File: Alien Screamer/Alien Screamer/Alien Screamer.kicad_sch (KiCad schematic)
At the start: 61 parts, among them J1 AudioJack2, Q1 2N3904, Q2 2N3904, Q3 Q_NJFET_DSG, SW1 PWR, SW2 LFO_Shaping, SW3 LFO_Shaping, SW4 SYNC, U1 LM324, U2 LM386

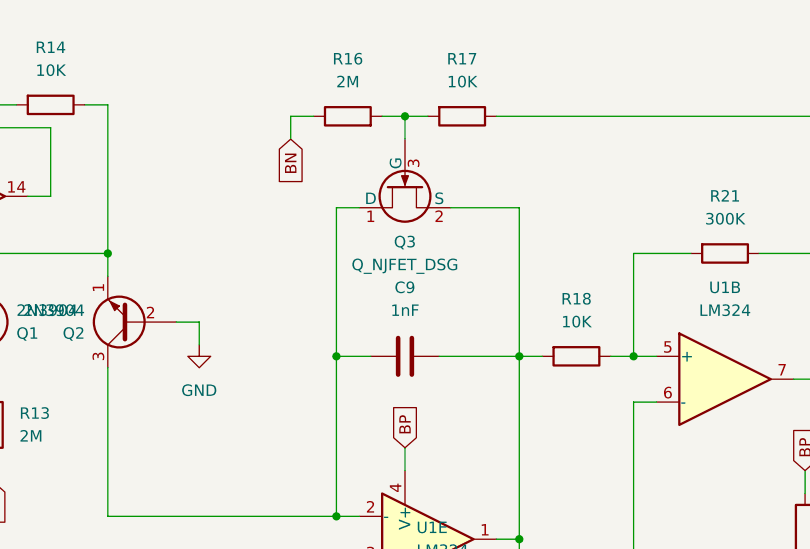
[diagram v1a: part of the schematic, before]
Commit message: Alien Screamer - changing resistor's sizes
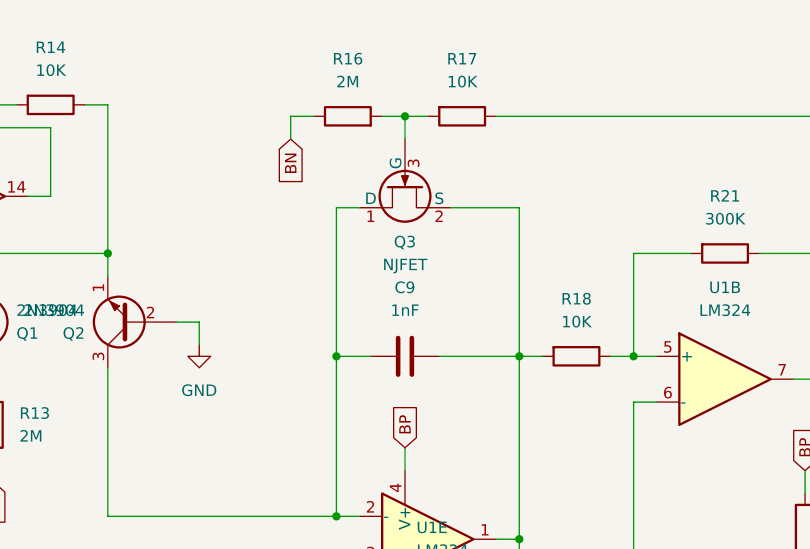
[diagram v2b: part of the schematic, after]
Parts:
- Q3: value Q_NJFET_DSG -> NJFET
- R1, R10, R11, R12, R13, R14, R15, R16, R17, R18, R19, R2, R20, R21, R22, R23, R24, R3, R4, R5, R6, R7, R8, R9: footprint Resistor_THT:R_Axial_DIN0204_L3.6mm_D1.6mm_P5.08mm_Horizontal -> Resistor_THT:R_Axial_DIN0207_L6.3mm_D2.5mm_P7.62mm_Horizontal
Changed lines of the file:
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@@
       (effects (font (size 1.27 1.27)) (justify left))
     )
-    (property "Footprint" "Resistor_THT:R_Axial_DIN0204_L3.6mm_D1.6mm_P5.08mm_Horizontal" (at 117.602 57.15 90)
+    (property "Footprint" "Resistor_THT:R_Axial_DIN0207_L6.3mm_D2.5mm_P7.62mm_Horizontal" (at 117.602 57.15 90)
       (effects (font (size 1.27 1.27)) hide)
     )
@@
       (effects (font (size 1.27 1.27)))
     )
-    (property "Footprint" "Resistor_THT:R_Axial_DIN0204_L3.6mm_D1.6mm_P5.08mm_Horizontal" (at 102.87 49.022 90)
+    (property "Footprint" "Resistor_THT:R_Axial_DIN0207_L6.3mm_D2.5mm_P7.62mm_Horizontal" (at 102.87 49.022 90)
       (effects (font (size 1.27 1.27)) hide)
     )
@@
       (effects (font (size 1.27 1.27)))
     )
-    (property "Footprint" "Resistor_THT:R_Axial_DIN0204_L3.6mm_D1.6mm_P5.08mm_Horizontal" (at 142.24 19.812 90)
+    (property "Footprint" "Resistor_THT:R_Axial_DIN0207_L6.3mm_D2.5mm_P7.62mm_Horizontal" (at 142.24 19.812 90)
       (effects (font (size 1.27 1.27)) hide)
     )
@@
       (effects (font (size 1.27 1.27)) (justify right))
     )
-    (property "Footprint" "Resistor_THT:R_Axial_DIN0204_L3.6mm_D1.6mm_P5.08mm_Horizontal" (at 18.288 63.5 90)
+    (property "Footprint" "Resistor_THT:R_Axial_DIN0207_L6.3mm_D2.5mm_P7.62mm_Horizontal" (at 18.288 63.5 90)
       (effects (font (size 1.27 1.27)) hide)
     )
@@
       (effects (font (size 1.27 1.27)) (justify right))
     )
-    (property "Footprint" "Resistor_THT:R_Axial_DIN0204_L3.6mm_D1.6mm_P5.08mm_Horizontal" (at 50.038 180.34 90)
+    (property "Footprint" "Resistor_THT:R_Axial_DIN0207_L6.3mm_D2.5mm_P7.62mm_Horizontal" (at 50.038 180.34 90)
       (effects (font (size 1.27 1.27)) hide)
     )
@@
       (effects (font (size 1.27 1.27)) (justify right))
     )
-    (property "Footprint" "Resistor_THT:R_Axial_DIN0204_L3.6mm_D1.6mm_P5.08mm_Horizontal" (at 227.838 78.74 90)
+    (property "Footprint" "Resistor_THT:R_Axial_DIN0207_L6.3mm_D2.5mm_P7.62mm_Horizontal" (at 227.838 78.74 90)
       (effects (font (size 1.27 1.27)) hide)
     )
@@
       (effects (font (size 1.27 1.27)))
     )
-    (property "Footprint" "Resistor_THT:R_Axial_DIN0204_L3.6mm_D1.6mm_P5.08mm_Horizontal" (at 200.66 47.752 90)
+    (property "Footprint" "Resistor_THT:R_Axial_DIN0207_L6.3mm_D2.5mm_P7.62mm_Horizontal" (at 200.66 47.752 90)
       (effects (font (size 1.27 1.27)) hide)
     )
@@
       (effects (font (size 1.27 1.27)))
     )
-    (property "Footprint" "Resistor_THT:R_Axial_DIN0204_L3.6mm_D1.6mm_P5.08mm_Horizontal" (at 175.26 24.638 90)
+    (property "Footprint" "Resistor_THT:R_Axial_DIN0207_L6.3mm_D2.5mm_P7.62mm_Horizontal" (at 175.26 24.638 90)
       (effects (font (size 1.27 1.27)) hide)
     )
@@
       (effects (font (size 1.27 1.27)) (justify left))
     )
-    (property "Footprint" "Resistor_THT:R_Axial_DIN0204_L3.6mm_D1.6mm_P5.08mm_Horizontal" (at 107.442 57.15 90)
+    (property "Footprint" "Resistor_THT:R_Axial_DIN0207_L6.3mm_D2.5mm_P7.62mm_Horizontal" (at 107.442 57.15 90)
       (effects (font (size 1.27 1.27)) hide)
     )
@@
       (effects (font (size 1.27 1.27)) (justify right))
     )
-    (property "Footprint" "Resistor_THT:R_Axial_DIN0204_L3.6mm_D1.6mm_P5.08mm_Horizontal" (at 251.968 151.13 90)
+    (property "Footprint" "Resistor_THT:R_Axial_DIN0207_L6.3mm_D2.5mm_P7.62mm_Horizontal" (at 251.968 151.13 90)
       (effects (font (size 1.27 1.27)) hide)
     )
@@
       (effects (font (size 1.27 1.27)) (justify right))
     )
-    (property "Footprint" "Resistor_THT:R_Axial_DIN0204_L3.6mm_D1.6mm_P5.08mm_Horizontal" (at 227.838 68.58 90)
+    (property "Footprint" "Resistor_THT:R_Axial_DIN0207_L6.3mm_D2.5mm_P7.62mm_Horizontal" (at 227.838 68.58 90)
       (effects (font (size 1.27 1.27)) hide)
     )
@@
       (effects (font (size 1.27 1.27)))
     )
-    (property "Footprint" "Resistor_THT:R_Axial_DIN0204_L3.6mm_D1.6mm_P5.08mm_Horizontal" (at 62.23 50.292 90)
+    (property "Footprint" "Resistor_THT:R_Axial_DIN0207_L6.3mm_D2.5mm_P7.62mm_Horizontal" (at 62.23 50.292 90)
       (effects (font (size 1.27 1.27)) hide)
     )
@@
       (effects (font (size 1.27 1.27)))
     )
-    (property "Footprint" "Resistor_THT:R_Axial_DIN0204_L3.6mm_D1.6mm_P5.08mm_Horizontal" (at 102.87 22.352 90)
+    (property "Footprint" "Resistor_THT:R_Axial_DIN0207_L6.3mm_D2.5mm_P7.62mm_Horizontal" (at 102.87 22.352 90)
       (effects (font (size 1.27 1.27)) hide)
     )
@@
       (effects (font (size 1.27 1.27)))
     )
-    (property "Footprint" "Resistor_THT:R_Axial_DIN0204_L3.6mm_D1.6mm_P5.08mm_Horizontal" (at 31.75 23.368 90)
+    (property "Footprint" "Resistor_THT:R_Axial_DIN0207_L6.3mm_D2.5mm_P7.62mm_Horizontal" (at 31.75 23.368 90)
       (effects (font (size 1.27 1.27)) hide)
     )
@@
       (effects (font (size 1.27 1.27)) (justify left))
     )
-    (property "Footprint" "Resistor_THT:R_Axial_DIN0204_L3.6mm_D1.6mm_P5.08mm_Horizontal" (at 134.112 57.15 90)
+    (property "Footprint" "Resistor_THT:R_Axial_DIN0207_L6.3mm_D2.5mm_P7.62mm_Horizontal" (at 134.112 57.15 90)
       (effects (font (size 1.27 1.27)) hide)
     )
@@
       (effects (font (size 1.27 1.27)) (justify right))
     )
-    (property "Footprint" "Resistor_THT:R_Axial_DIN0204_L3.6mm_D1.6mm_P5.08mm_Horizontal" (at 39.878 64.77 90)
+    (property "Footprint" "Resistor_THT:R_Axial_DIN0207_L6.3mm_D2.5mm_P7.62mm_Horizontal" (at 39.878 64.77 90)
       (effects (font (size 1.27 1.27)) hide)
     )
@@
       (effects (font (size 1.27 1.27)))
     )
-    (property "Footprint" "Resistor_THT:R_Axial_DIN0204_L3.6mm_D1.6mm_P5.08mm_Horizontal" (at 31.75 56.642 90)
+    (property "Footprint" "Resistor_THT:R_Axial_DIN0207_L6.3mm_D2.5mm_P7.62mm_Horizontal" (at 31.75 56.642 90)
       (effects (font (size 1.27 1.27)) hide)
     )
@@
       (effects (font (size 1.27 1.27)))
     )
-    (property "Footprint" "Resistor_THT:R_Axial_DIN0204_L3.6mm_D1.6mm_P5.08mm_Horizontal" (at 217.17 36.322 90)
+    (property "Footprint" "Resistor_THT:R_Axial_DIN0207_L6.3mm_D2.5mm_P7.62mm_Horizontal" (at 217.17 36.322 90)
       (effects (font (size 1.27 1.27)) hide)
     )
@@
       (effects (font (size 1.27 1.27)) (justify right))
     )
-    (property "Footprint" "Resistor_THT:R_Axial_DIN0204_L3.6mm_D1.6mm_P5.08mm_Horizontal" (at 213.868 138.43 90)
+    (property "Footprint" "Resistor_THT:R_Axial_DIN0207_L6.3mm_D2.5mm_P7.62mm_Horizontal" (at 213.868 138.43 90)
       (effects (font (size 1.27 1.27)) hide)
     )
@@
       (effects (font (size 1.27 1.27)) (justify right))
     )
-    (property "Footprint" "Resistor_THT:R_Axial_DIN0204_L3.6mm_D1.6mm_P5.08mm_Horizontal" (at 18.288 53.34 90)
+    (property "Footprint" "Resistor_THT:R_Axial_DIN0207_L6.3mm_D2.5mm_P7.62mm_Horizontal" (at 18.288 53.34 90)
       (effects (font (size 1.27 1.27)) hide)
     )
@@
       (effects (font (size 1.27 1.27)) (justify right))
     )
-    (property "Footprint" "Resistor_THT:R_Axial_DIN0204_L3.6mm_D1.6mm_P5.08mm_Horizontal" (at 144.018 96.52 90)
+    (property "Footprint" "Resistor_THT:R_Axial_DIN0207_L6.3mm_D2.5mm_P7.62mm_Horizontal" (at 144.018 96.52 90)
       (effects (font (size 1.27 1.27)) hide)
     )
@@
       (effects (font (size 1.27 1.27)))
     )
-    (property "Value" "Q_NJFET_DSG" (at 181.61 39.37 90)
+    (property "Value" "NJFET" (at 181.61 39.37 90)
       (effects (font (size 1.27 1.27)))
     )
@@
       (effects (font (size 1.27 1.27)) (justify right))
     )
-    (property "Footprint" "Resistor_THT:R_Axial_DIN0204_L3.6mm_D1.6mm_P5.08mm_Horizontal" (at 50.038 165.1 90)
+    (property "Footprint" "Resistor_THT:R_Axial_DIN0207_L6.3mm_D2.5mm_P7.62mm_Horizontal" (at 50.038 165.1 90)
       (effects (font (size 1.27 1.27)) hide)
     )
@@
       (effects (font (size 1.27 1.27)))
     )
-    (property "Footprint" "Resistor_THT:R_Axial_DIN0204_L3.6mm_D1.6mm_P5.08mm_Horizontal" (at 205.74 130.302 90)
+    (property "Footprint" "Resistor_THT:R_Axial_DIN0207_L6.3mm_D2.5mm_P7.62mm_Horizontal" (at 205.74 130.302 90)
       (effects (font (size 1.27 1.27)) hide)
     )
@@
       (effects (font (size 1.27 1.27)))
     )
-    (property "Footprint" "Resistor_THT:R_Axial_DIN0204_L3.6mm_D1.6mm_P5.08mm_Horizontal" (at 187.96 21.082 90)
-      (effects (font (size 1.27 1.27)) hide)
-    )
+    (property "Footprint" "Resistor_THT:R_Axial_DIN0207_L6.3mm_D2.5mm_P7.62mm_Horizontal" (at 187.96 21.082 90)
+      (effects (font (size 1.27 1.27)) hide)
+    )

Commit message: Alien Screamer - changed resistors sizes
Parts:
- R1, R10, R11, R12, R13, R14, R15, R16, R17, R18, R19, R2, R20, R21, R22, R23, R24, R3, R4, R5, R6, R7, R8, R9: footprint Resistor_THT:R_Axial_DIN0207_L6.3mm_D2.5mm_P7.62mm_Horizontal -> Library:R_Axial_DIN0207_L6.3mm_D2.5mm_P7.62mm_Horizontal
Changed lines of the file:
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@@
       (effects (font (size 1.27 1.27)) (justify left))
     )
-    (property "Footprint" "Resistor_THT:R_Axial_DIN0207_L6.3mm_D2.5mm_P7.62mm_Horizontal" (at 117.602 57.15 90)
+    (property "Footprint" "Library:R_Axial_DIN0207_L6.3mm_D2.5mm_P7.62mm_Horizontal" (at 117.602 57.15 90)
       (effects (font (size 1.27 1.27)) hide)
     )
@@
       (effects (font (size 1.27 1.27)))
     )
-    (property "Footprint" "Resistor_THT:R_Axial_DIN0207_L6.3mm_D2.5mm_P7.62mm_Horizontal" (at 102.87 49.022 90)
+    (property "Footprint" "Library:R_Axial_DIN0207_L6.3mm_D2.5mm_P7.62mm_Horizontal" (at 102.87 49.022 90)
       (effects (font (size 1.27 1.27)) hide)
     )
@@
       (effects (font (size 1.27 1.27)))
     )
-    (property "Footprint" "Resistor_THT:R_Axial_DIN0207_L6.3mm_D2.5mm_P7.62mm_Horizontal" (at 142.24 19.812 90)
+    (property "Footprint" "Library:R_Axial_DIN0207_L6.3mm_D2.5mm_P7.62mm_Horizontal" (at 142.24 19.812 90)
       (effects (font (size 1.27 1.27)) hide)
     )
@@
       (effects (font (size 1.27 1.27)) (justify right))
     )
-    (property "Footprint" "Resistor_THT:R_Axial_DIN0207_L6.3mm_D2.5mm_P7.62mm_Horizontal" (at 18.288 63.5 90)
+    (property "Footprint" "Library:R_Axial_DIN0207_L6.3mm_D2.5mm_P7.62mm_Horizontal" (at 18.288 63.5 90)
       (effects (font (size 1.27 1.27)) hide)
     )
@@
       (effects (font (size 1.27 1.27)) (justify right))
     )
-    (property "Footprint" "Resistor_THT:R_Axial_DIN0207_L6.3mm_D2.5mm_P7.62mm_Horizontal" (at 50.038 180.34 90)
+    (property "Footprint" "Library:R_Axial_DIN0207_L6.3mm_D2.5mm_P7.62mm_Horizontal" (at 50.038 180.34 90)
       (effects (font (size 1.27 1.27)) hide)
     )
@@
       (effects (font (size 1.27 1.27)) (justify right))
     )
-    (property "Footprint" "Resistor_THT:R_Axial_DIN0207_L6.3mm_D2.5mm_P7.62mm_Horizontal" (at 227.838 78.74 90)
+    (property "Footprint" "Library:R_Axial_DIN0207_L6.3mm_D2.5mm_P7.62mm_Horizontal" (at 227.838 78.74 90)
       (effects (font (size 1.27 1.27)) hide)
     )
@@
       (effects (font (size 1.27 1.27)))
     )
-    (property "Footprint" "Resistor_THT:R_Axial_DIN0207_L6.3mm_D2.5mm_P7.62mm_Horizontal" (at 200.66 47.752 90)
+    (property "Footprint" "Library:R_Axial_DIN0207_L6.3mm_D2.5mm_P7.62mm_Horizontal" (at 200.66 47.752 90)
       (effects (font (size 1.27 1.27)) hide)
     )
@@
       (effects (font (size 1.27 1.27)))
     )
-    (property "Footprint" "Resistor_THT:R_Axial_DIN0207_L6.3mm_D2.5mm_P7.62mm_Horizontal" (at 175.26 24.638 90)
+    (property "Footprint" "Library:R_Axial_DIN0207_L6.3mm_D2.5mm_P7.62mm_Horizontal" (at 175.26 24.638 90)
       (effects (font (size 1.27 1.27)) hide)
     )
@@
       (effects (font (size 1.27 1.27)) (justify left))
     )
-    (property "Footprint" "Resistor_THT:R_Axial_DIN0207_L6.3mm_D2.5mm_P7.62mm_Horizontal" (at 107.442 57.15 90)
+    (property "Footprint" "Library:R_Axial_DIN0207_L6.3mm_D2.5mm_P7.62mm_Horizontal" (at 107.442 57.15 90)
       (effects (font (size 1.27 1.27)) hide)
     )
@@
       (effects (font (size 1.27 1.27)) (justify right))
     )
-    (property "Footprint" "Resistor_THT:R_Axial_DIN0207_L6.3mm_D2.5mm_P7.62mm_Horizontal" (at 251.968 151.13 90)
+    (property "Footprint" "Library:R_Axial_DIN0207_L6.3mm_D2.5mm_P7.62mm_Horizontal" (at 251.968 151.13 90)
       (effects (font (size 1.27 1.27)) hide)
     )
@@
       (effects (font (size 1.27 1.27)) (justify right))
     )
-    (property "Footprint" "Resistor_THT:R_Axial_DIN0207_L6.3mm_D2.5mm_P7.62mm_Horizontal" (at 227.838 68.58 90)
+    (property "Footprint" "Library:R_Axial_DIN0207_L6.3mm_D2.5mm_P7.62mm_Horizontal" (at 227.838 68.58 90)
       (effects (font (size 1.27 1.27)) hide)
     )
@@
       (effects (font (size 1.27 1.27)))
     )
-    (property "Footprint" "Resistor_THT:R_Axial_DIN0207_L6.3mm_D2.5mm_P7.62mm_Horizontal" (at 62.23 50.292 90)
+    (property "Footprint" "Library:R_Axial_DIN0207_L6.3mm_D2.5mm_P7.62mm_Horizontal" (at 62.23 50.292 90)
       (effects (font (size 1.27 1.27)) hide)
     )
@@
       (effects (font (size 1.27 1.27)))
     )
-    (property "Footprint" "Resistor_THT:R_Axial_DIN0207_L6.3mm_D2.5mm_P7.62mm_Horizontal" (at 102.87 22.352 90)
+    (property "Footprint" "Library:R_Axial_DIN0207_L6.3mm_D2.5mm_P7.62mm_Horizontal" (at 102.87 22.352 90)
       (effects (font (size 1.27 1.27)) hide)
     )
@@
       (effects (font (size 1.27 1.27)))
     )
-    (property "Footprint" "Resistor_THT:R_Axial_DIN0207_L6.3mm_D2.5mm_P7.62mm_Horizontal" (at 31.75 23.368 90)
+    (property "Footprint" "Library:R_Axial_DIN0207_L6.3mm_D2.5mm_P7.62mm_Horizontal" (at 31.75 23.368 90)
       (effects (font (size 1.27 1.27)) hide)
     )
@@
       (effects (font (size 1.27 1.27)) (justify left))
     )
-    (property "Footprint" "Resistor_THT:R_Axial_DIN0207_L6.3mm_D2.5mm_P7.62mm_Horizontal" (at 134.112 57.15 90)
+    (property "Footprint" "Library:R_Axial_DIN0207_L6.3mm_D2.5mm_P7.62mm_Horizontal" (at 134.112 57.15 90)
       (effects (font (size 1.27 1.27)) hide)
     )
@@
       (effects (font (size 1.27 1.27)) (justify right))
     )
-    (property "Footprint" "Resistor_THT:R_Axial_DIN0207_L6.3mm_D2.5mm_P7.62mm_Horizontal" (at 39.878 64.77 90)
+    (property "Footprint" "Library:R_Axial_DIN0207_L6.3mm_D2.5mm_P7.62mm_Horizontal" (at 39.878 64.77 90)
       (effects (font (size 1.27 1.27)) hide)
     )
@@
       (effects (font (size 1.27 1.27)))
     )
-    (property "Footprint" "Resistor_THT:R_Axial_DIN0207_L6.3mm_D2.5mm_P7.62mm_Horizontal" (at 31.75 56.642 90)
+    (property "Footprint" "Library:R_Axial_DIN0207_L6.3mm_D2.5mm_P7.62mm_Horizontal" (at 31.75 56.642 90)
       (effects (font (size 1.27 1.27)) hide)
     )
@@
       (effects (font (size 1.27 1.27)))
     )
-    (property "Footprint" "Resistor_THT:R_Axial_DIN0207_L6.3mm_D2.5mm_P7.62mm_Horizontal" (at 217.17 36.322 90)
+    (property "Footprint" "Library:R_Axial_DIN0207_L6.3mm_D2.5mm_P7.62mm_Horizontal" (at 217.17 36.322 90)
       (effects (font (size 1.27 1.27)) hide)
     )
@@
       (effects (font (size 1.27 1.27)) (justify right))
     )
-    (property "Footprint" "Resistor_THT:R_Axial_DIN0207_L6.3mm_D2.5mm_P7.62mm_Horizontal" (at 213.868 138.43 90)
+    (property "Footprint" "Library:R_Axial_DIN0207_L6.3mm_D2.5mm_P7.62mm_Horizontal" (at 213.868 138.43 90)
       (effects (font (size 1.27 1.27)) hide)
     )
@@
       (effects (font (size 1.27 1.27)) (justify right))
     )
-    (property "Footprint" "Resistor_THT:R_Axial_DIN0207_L6.3mm_D2.5mm_P7.62mm_Horizontal" (at 18.288 53.34 90)
+    (property "Footprint" "Library:R_Axial_DIN0207_L6.3mm_D2.5mm_P7.62mm_Horizontal" (at 18.288 53.34 90)
       (effects (font (size 1.27 1.27)) hide)
     )
@@
       (effects (font (size 1.27 1.27)) (justify right))
     )
-    (property "Footprint" "Resistor_THT:R_Axial_DIN0207_L6.3mm_D2.5mm_P7.62mm_Horizontal" (at 144.018 96.52 90)
+    (property "Footprint" "Library:R_Axial_DIN0207_L6.3mm_D2.5mm_P7.62mm_Horizontal" (at 144.018 96.52 90)
       (effects (font (size 1.27 1.27)) hide)
     )
@@
       (effects (font (size 1.27 1.27)) (justify right))
     )
-    (property "Footprint" "Resistor_THT:R_Axial_DIN0207_L6.3mm_D2.5mm_P7.62mm_Horizontal" (at 50.038 165.1 90)
+    (property "Footprint" "Library:R_Axial_DIN0207_L6.3mm_D2.5mm_P7.62mm_Horizontal" (at 50.038 165.1 90)
       (effects (font (size 1.27 1.27)) hide)
     )
@@
       (effects (font (size 1.27 1.27)))
     )
-    (property "Footprint" "Resistor_THT:R_Axial_DIN0207_L6.3mm_D2.5mm_P7.62mm_Horizontal" (at 205.74 130.302 90)
+    (property "Footprint" "Library:R_Axial_DIN0207_L6.3mm_D2.5mm_P7.62mm_Horizontal" (at 205.74 130.302 90)
       (effects (font (size 1.27 1.27)) hide)
     )
@@
       (effects (font (size 1.27 1.27)))
     )
-    (property "Footprint" "Resistor_THT:R_Axial_DIN0207_L6.3mm_D2.5mm_P7.62mm_Horizontal" (at 187.96 21.082 90)
-      (effects (font (size 1.27 1.27)) hide)
-    )
+    (property "Footprint" "Library:R_Axial_DIN0207_L6.3mm_D2.5mm_P7.62mm_Horizontal" (at 187.96 21.082 90)
+      (effects (font (size 1.27 1.27)) hide)
+    )

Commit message: AlienScream - fixed a few values
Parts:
- R20, R5: value 100K -> 4.7K
- R6, R7: value 3K -> 4.7K
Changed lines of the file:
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@@
     (stroke (width 0) (type default))
   )
-  (wire (pts (xy 58.42 171.45) (xy 58.42 172.72))
+  (wire (pts (xy 58.42 165.1) (xy 58.42 172.72))
     (stroke (width 0) (type default))
   )
@@
       (effects (font (size 1.27 1.27)) (justify right))
     )
-    (property "Value" "3K" (at 50.8 181.61 0)
+    (property "Value" "4.7K" (at 50.8 181.61 0)
       (effects (font (size 1.27 1.27)) (justify right))
     )
@@
       (effects (font (size 1.27 1.27)) (justify right))
     )
-    (property "Value" "100K" (at 40.64 66.04 0)
+    (property "Value" "4.7K" (at 40.64 66.04 0)
       (effects (font (size 1.27 1.27)) (justify right))
     )
@@
       (effects (font (size 1.27 1.27)) (justify right))
     )
-    (property "Value" "100K" (at 214.63 139.7 0)
+    (property "Value" "4.7K" (at 214.63 139.7 0)
       (effects (font (size 1.27 1.27)) (justify right))
     )
@@
     )
   )
-  (symbol (lib_id "power:PWR_FLAG") (at 58.42 171.45 0) (unit 1)
-    (in_bom yes) (on_board yes) (dnp no) (fields_autoplaced)
-    (property "Reference" "#FLG04" (at 58.42 169.545 0)
-      (effects (font (size 1.27 1.27)) hide)
-    )
-    (property "Value" "PWR_FLAG" (at 58.42 166.37 0)
-      (effects (font (size 1.27 1.27)))
-    )
-    (property "Footprint" "" (at 58.42 171.45 0)
-      (effects (font (size 1.27 1.27)) hide)
-    )
-    (property "Datasheet" "~" (at 58.42 171.45 0)
+  (symbol (lib_id "power:PWR_FLAG") (at 58.42 165.1 0) (unit 1)
+    (in_bom yes) (on_board yes) (dnp no) (fields_autoplaced)
+    (property "Reference" "#FLG04" (at 58.42 163.195 0)
+      (effects (font (size 1.27 1.27)) hide)
+    )
+    (property "Value" "PWR_FLAG" (at 58.42 160.02 0)
+      (effects (font (size 1.27 1.27)))
+    )
+    (property "Footprint" "" (at 58.42 165.1 0)
+      (effects (font (size 1.27 1.27)) hide)
+    )
+    (property "Datasheet" "~" (at 58.42 165.1 0)
       (effects (font (size 1.27 1.27)) hide)
     )
@@
       (effects (font (size 1.27 1.27)) (justify right))
     )
-    (property "Value" "3K" (at 50.8 166.37 0)
-      (effects (font (size 1.27 1.27)) (justify right))
-    )
+    (property "Value" "4.7K" (at 50.8 166.37 0)
+      (effects (font (size 1.27 1.27)) (justify right))
+    )

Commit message: Alien Screamer - misc fixes
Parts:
- Q3: value NJFET -> 2N5457
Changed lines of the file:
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@@
       (effects (font (size 1.27 1.27)))
     )
-    (property "Value" "NJFET" (at 181.61 39.37 90)
+    (property "Value" "2N5457" (at 181.61 39.37 90)
       (effects (font (size 1.27 1.27)))
     )

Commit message: minor fixes and cleanups
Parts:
- added J2: Conn_01x03, Connector_PinHeader_2.54mm:PinHeader_1x03_P2.54mm_Vertical, symbol Connector_Generic:Conn_01x03
- H1, H2, H3, H4: now left out of the parts list
- LFO_SHAPING1: renamed from SW2; value LFO_Shaping -> SW_SPDT
- LFO_SHAPING2: renamed from SW3; value LFO_Shaping -> SW_SPDT
- PWR1: renamed from SW1; value PWR -> SW_SPDT
- SYNC1: renamed from SW4; value SYNC -> SW_SPDT
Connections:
- net BN: now also J2.3 (Pin_3)
- net BP: now also J2.1 (Pin_1)
- net GND: now also J2.2 (Pin_2)
